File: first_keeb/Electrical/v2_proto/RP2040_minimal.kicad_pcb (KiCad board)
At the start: 2 copper layers, 80 x 60 mm, 67 parts, among them P1 USB_C_Receptacle_GCT_USB4105-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, Q1 SOT-23, SW1 2-1825027-0_Right_Angle_Switc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, SW2 2-1825027-0_Right_Angle_Switc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, U1 NCP1117-3.3_SOT223, U2 SOT-23, U3 RP2040, U3 W25Q128JVS, U5 SOT143B, Y1 ABLS-12.000MHZ-B4-T

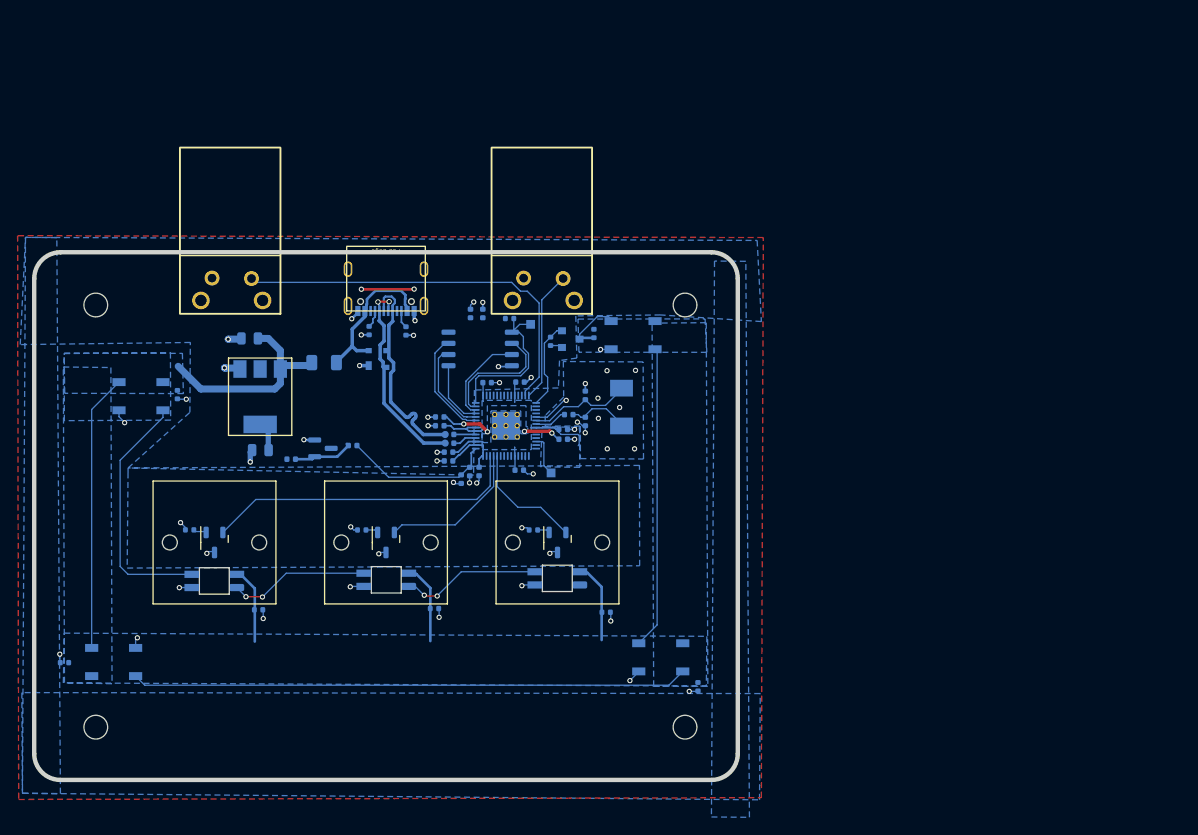
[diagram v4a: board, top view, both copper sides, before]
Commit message: finishes proto_v2 board. Set up some stuff to automate jlcpcb format for pcb assembly
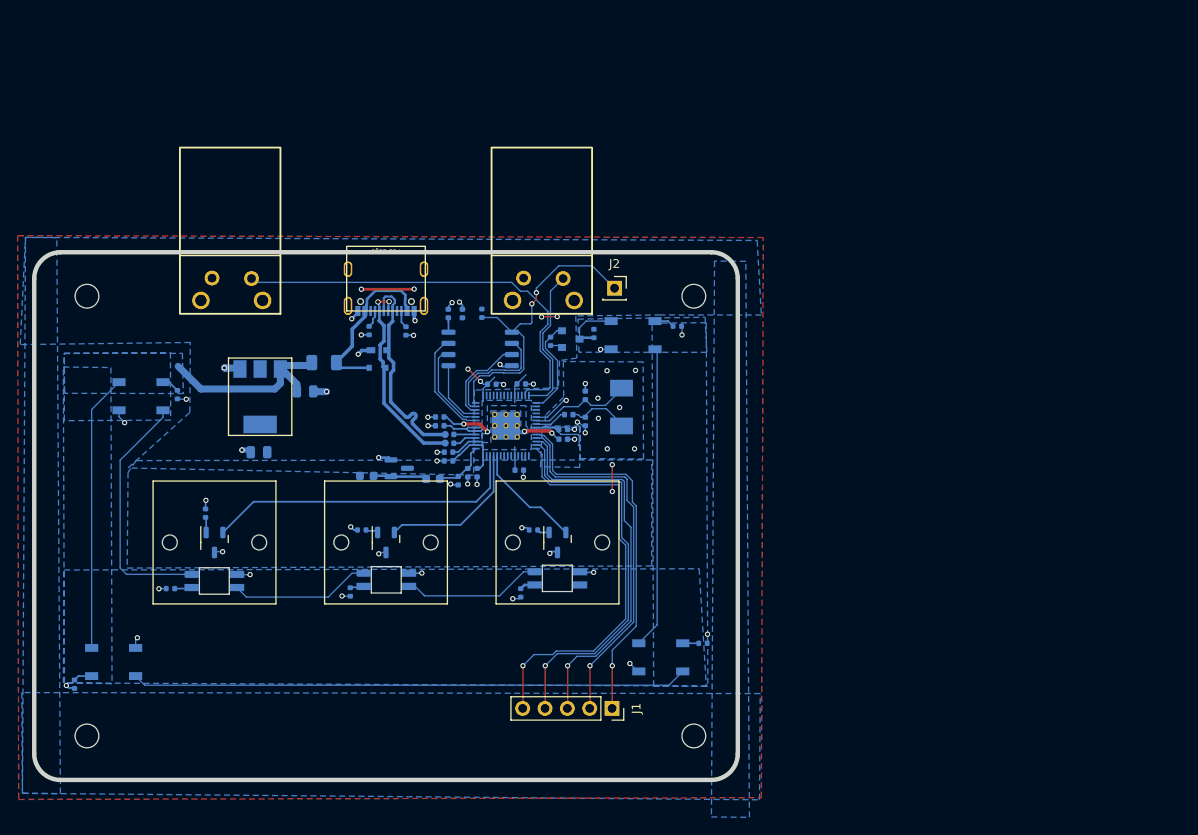
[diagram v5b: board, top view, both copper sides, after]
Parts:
- removed the C19 at (85.5, 137.7)
- removed the C20 at (105.5, 137.5)
- removed TP1: TestPoint_Pad_1.0x1.0mm, TestPoint:TestPoint_Pad_1.0x1.0mm
- removed TP2: RUN, TestPoint:TestPoint_Pad_1.0x1.0mm
- added C22: 1u, Capacitor_SMD:C_0402_1005Metric, B.Cu at (133.1, 105.4)
- added C26: 1u, Capacitor_SMD:C_0402_1005Metric, B.Cu at (75.5, 135.2)
- added C27: 1u, Capacitor_SMD:C_0402_1005Metric, B.Cu at (95.9, 135.6)
- added J1: Conn_01x05_Socket, Connector_PinSocket_2.54mm:PinSocket_1x05_P2.54mm_Vertical, F.Cu at (125.7, 148.9)
- added J2: Conn_01x01_Socket, Connector_PinSocket_2.54mm:PinSocket_1x01_P2.54mm_Vertical, F.Cu at (126.0, 101.1)
- C16: value 100n -> 1u
- C19: renamed from C21; value C_0402_1005Metric -> 1u
- C20: renamed from C22; value C_0402_1005Metric -> 1u
- C21: renamed from C23; value C_0402_1005Metric -> 1u
- C23: renamed from C26; value C_0402_1005Metric -> 1u
- C24: renamed from C25; value C_0402_1005Metric -> 1u
- C25: renamed from C24; value C_0402_1005Metric -> 1u
- C28: value C_0402_1005Metric -> 1u
- C8: renamed from C3; value 1u -> 100n
- D5: renamed from D1; value SK6812-MINI-E -> SK6812MINI
- D6: renamed from D2; value SK6812-MINI-E -> SK6812MINI
- D7: value SK6812-MINI-E -> SK6812MINI
- F1: value Fuse_1206_3216Metric -> 0ZCJ0025AF2E
- P1: value USB_C_Receptacle_GCT_USB4105-xx-A_16P_TopMnt_Horizontal -> USB4105-GF-A
- Q1: value SOT-23 -> BSS138
- R1: footprint Capacitor_SMD:C_0402_1005Metric -> Capacitor_SMD:C_0603_1608Metric
- R10, R9: value C_0402_1005Metric -> 10k
- R2: renamed from R7; value C_0402_1005Metric -> 5.1k
- R3: renamed from R8; value C_0402_1005Metric -> 5.1k
- R4: renamed from R2; footprint Capacitor_SMD:C_0402_1005Metric -> Capacitor_SMD:C_0603_1608Metric
- R5: renamed from R3; value 27 -> 27R
- R6: renamed from R4; value 27 -> 27R
- R7: renamed from R5; value C_0402_1005Metric -> 10k
- SW1, SW2: value 2-1825027-0_Right_Angle_Switch-9.24mm_Stem -> SW_Push
- U2: value SOT-23 -> LM4040DBZ-3
- U3: renamed from U5; value SOT143B -> PRTR5V0U2X
- U4: renamed from U3; value W25Q128JVS -> W25Q32JVSS
- Y1: value ABLS-12.000MHZ-B4-T -> ABM7-12.000MHZ-D2Y-T
- moved C28 9.96 mm to (115.3, 135.7), turned to -90 degrees
- moved R4 9.89 mm to (105.3, 122.8)
- moved U2 8.96 mm to (101.5, 121.6)
- moved R1 8.80 mm to (97.8, 122.4)
- moved C1 8.71 mm to (90.8, 112.8), turned to 0 degrees
- moved C23 4.96 mm to (136.0, 141.5), turned to 0 degrees
- moved R7 3.21 mm to (110.9, 103.9), turned to -90 degrees
- moved C24 2.71 mm to (64.6, 146.1), turned to -90 degrees
- moved C21 2.62 mm to (79.5, 126.7), turned to -90 degrees
- moved C15 2.53 mm to (107.1, 104.0)
- moved C16 2.32 mm to (108.7, 104.0)
- moved REF** 1.41 mm to (66.0, 102.0)
- moved REF** 1.41 mm to (66.0, 152.0)
- moved REF** 1.41 mm to (135.0, 102.0)
- moved REF** 1.41 mm to (135.0, 152.0)
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- renumbered C10 to C1, C4 to C10, C12 to C11, C13 to C12, C7 to C13, C11 to C2, C1 to C3, C2 to C4, C9 to C5, C11 to C6, C12 to C7, C5 to C9, D6 to D1, D3 to D2, D4 to D3, D5 to D4, R6 to R8, U3 to U5
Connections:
- net /GPIO10 renamed BUTT0
- net /GPIO11 renamed BUTT1
- net /GPIO12 renamed LED_D_3V3
- net /GPIO26_ADC0 renamed RP_ADC0
- net /GPIO27_ADC1 renamed RP_ADC1
- net /GPIO28_ADC2 renamed RP_ADC2
- net CC1 renamed Net-(P1-CC1)
- net CC2 renamed Net-(P1-CC2)
- net DOUT_0 renamed Net-(D1-DOUT)
- net DOUT_1 renamed Net-(D2-DOUT)
- net DOUT_2 renamed Net-(D3-DOUT)
- C19 pad 1: +3V3 -> GND
- C19 pad 2: GND -> +3V3
- C20 pad 1: +3V3 -> GND
- C20 pad 2: GND -> +3V3
- C21 pad 1: +3V3 -> GND
- C21 pad 2: GND -> +3V3
- D4 pad 2: DOUT_3 -> Net-(D4-DOUT)
- D5 pad 1: DOUT_3 -> Net-(D5-DOUT)
- D5 pad 3: DOUT_4 -> Net-(D4-DOUT)
- D6 pad 1: DOUT_4 -> Net-(D6-DOUT)
- D6 pad 3: DOUT_5 -> Net-(D5-DOUT)
- D7 pad 1: DOUT_5 -> unconnected-(D7-DOUT-Pad1)
- D7 pad 3: DOUT_6 -> Net-(D6-DOUT)
- P1 pad A8: (no net) -> unconnected-(P1-SBU1-PadA8)
- P1 pad B8: (no net) -> unconnected-(P1-SBU2-PadB8)
- SW1 pad 3: GND -> (no net)
- SW1 pad 4: GND -> (no net)
- SW2 pad 3: GND -> (no net)
- SW2 pad 4: GND -> (no net)
- U3 pad 2: VBUS -> /USB_D+
- U3 pad 3: /USB_D+ -> /USB_D-
- U3 pad 4: /USB_D- -> VBUS
- U5 pad 24: /SWCLK -> SWCLK
- U5 pad 25: /SWD -> SWD
- U5 pad 26: /RUN -> RUN
- U5 pad 27: /GPIO16 -> UART0
- U5 pad 28: /GPIO17 -> UART1
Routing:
- net UART1: track 0.00 -> 46.9 mm, vias 0 -> 1
- net UART0: track 0.00 -> 45.6 mm, vias 0 -> 1
- net RUN: track 0.00 -> 44.1 mm, vias 0 -> 1
- net SWD: track 0.00 -> 42.5 mm, vias 0 -> 1
- net SWCLK: track 0.00 -> 42.1 mm, vias 0 -> 1
- net Net-(D4-DOUT): track 0.00 -> 28.4 mm
- net DOUT_3: track 28.3 -> 0.00 mm
- net /QSPI_SS: track 18.7 -> 36.8 mm, vias 0 -> 2
- net DOUT_5: track 16.1 -> 0.00 mm, vias 2 -> 0
- net Net-(D5-DOUT): track 0.00 -> 16.0 mm
- net DOUT_4: track 16.0 -> 0.00 mm, vias 2 -> 0
- net Net-(D6-DOUT): track 0.00 -> 16.0 mm
- net +5V: track 50.5 -> 36.0 mm
- net +3V3: track 43.0 -> 53.6 mm, vias 2 -> 8
- net ADC_AVDD: track 16.9 -> 6.44 mm
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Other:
- board text removed: "USB_BOOT"
